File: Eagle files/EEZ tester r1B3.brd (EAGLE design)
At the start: 84 x 76 mm, 91 parts, among them IC2 LM5574MTX/NOPB, K1 RT314005, Q1 2N7002, Q2 2N7002, Q3 2N7002, Q4 2N7002, Q5 2N7002, Q6 2N7002, SW1 1301.9316, SW2 1301.9316, X1 39303035, X3 SSW-113-02-S-D-RA, X4 ???, X6 09185166324

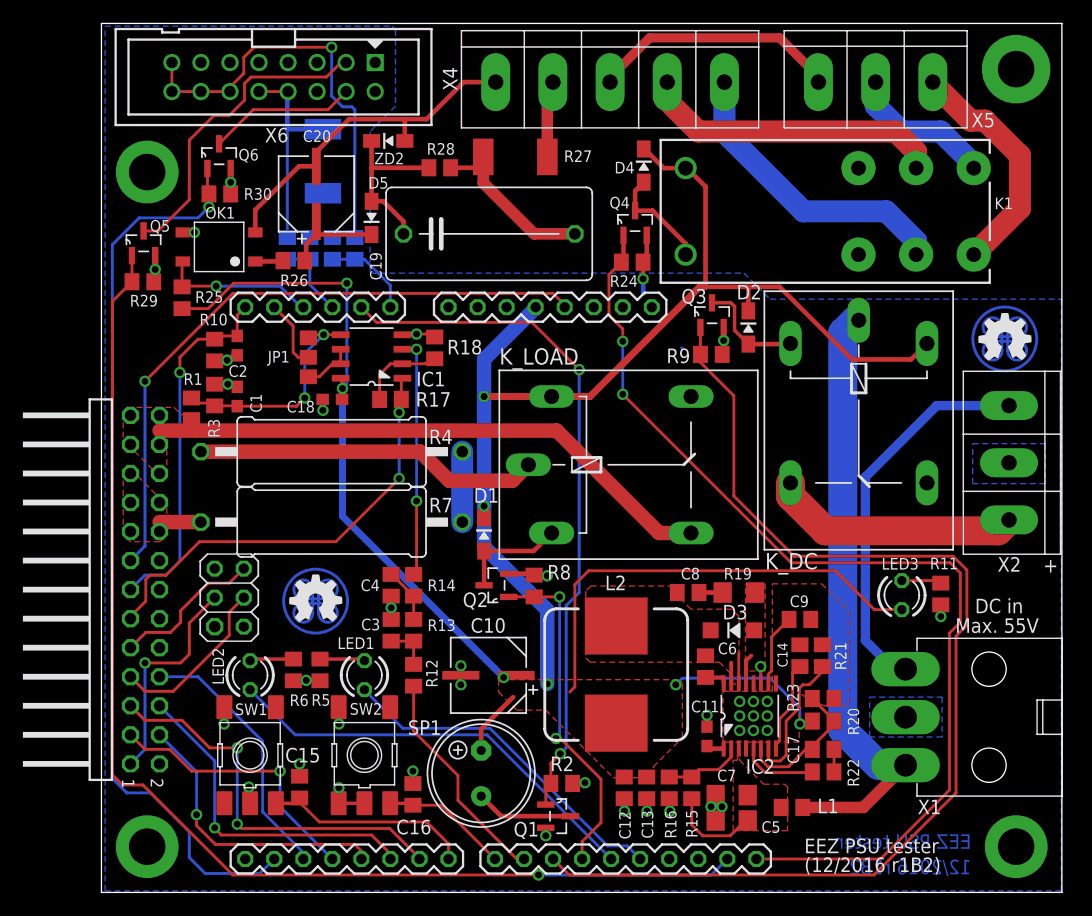
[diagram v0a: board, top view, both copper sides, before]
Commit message: Arduino rotated ICSP fixed
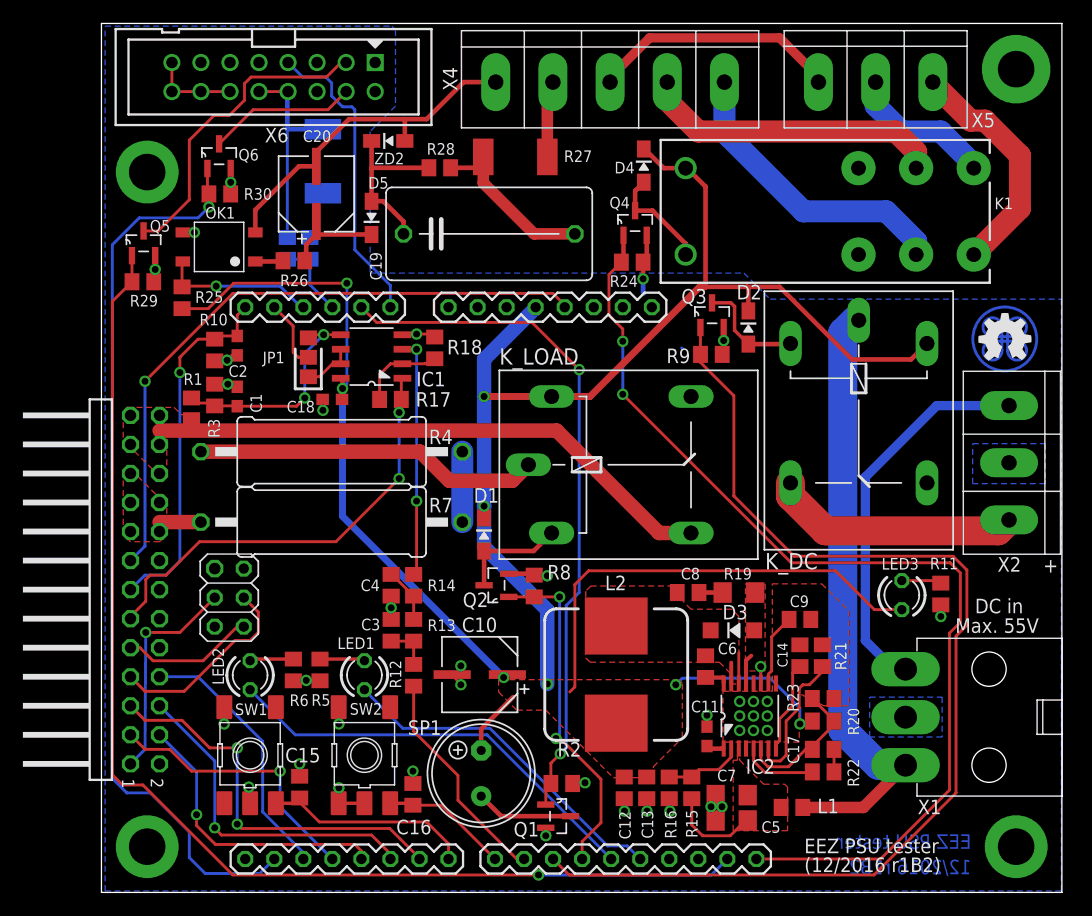
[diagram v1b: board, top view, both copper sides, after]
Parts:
- removed EEZ_SIGNATURE: SIGNATURESMALL, EEZ_Lib1:SIGNATURE_5MM
- removed R31: 10K, rcl:R0805
- removed R32: 3K2, rcl:R0805
- C17: value 4n7 -> 6n8
- C20: value 47u -> 220u
- L2: value 100uH -> 220uH
- R17: value (none) -> 10K
- R18: value (none) -> 20K
- R21: value 30K -> 18K
- R22: value 11K -> 20K
- R25: value 1K -> 2K2
- R26: value 330R -> 300R
- moved C10 0.76 mm to (33.1, 35.1)
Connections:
- net N$12 renamed LED_GREEN
- net N$14 renamed LED_RED
- net N$17 renamed SW2
- net N$18 renamed DC_ENABLE
- net N$6 renamed RPROG
- net N$8 renamed LOAD_ENABLE
- removed net +12V_AUX: MCU.A0, R31.1, R32.2
- new net AUX_DOUT2: MCU.A0, X6.7
- net GND: no longer R32.1
- net N$38: no longer R31.2
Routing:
- net N$38: track 37.1 -> 7.62 mm, vias 1 -> 0
- net AUX_DOUT2: track 0.00 -> 26.8 mm
- net +12V_AUX: track 7.93 -> 0.00 mm
- net MISO: track 15.0 -> 17.4 mm
- net SCLK: track 13.4 -> 11.6 mm
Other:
- board text removed: "R31"
- board text removed: "R32"

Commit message: parts value corrections
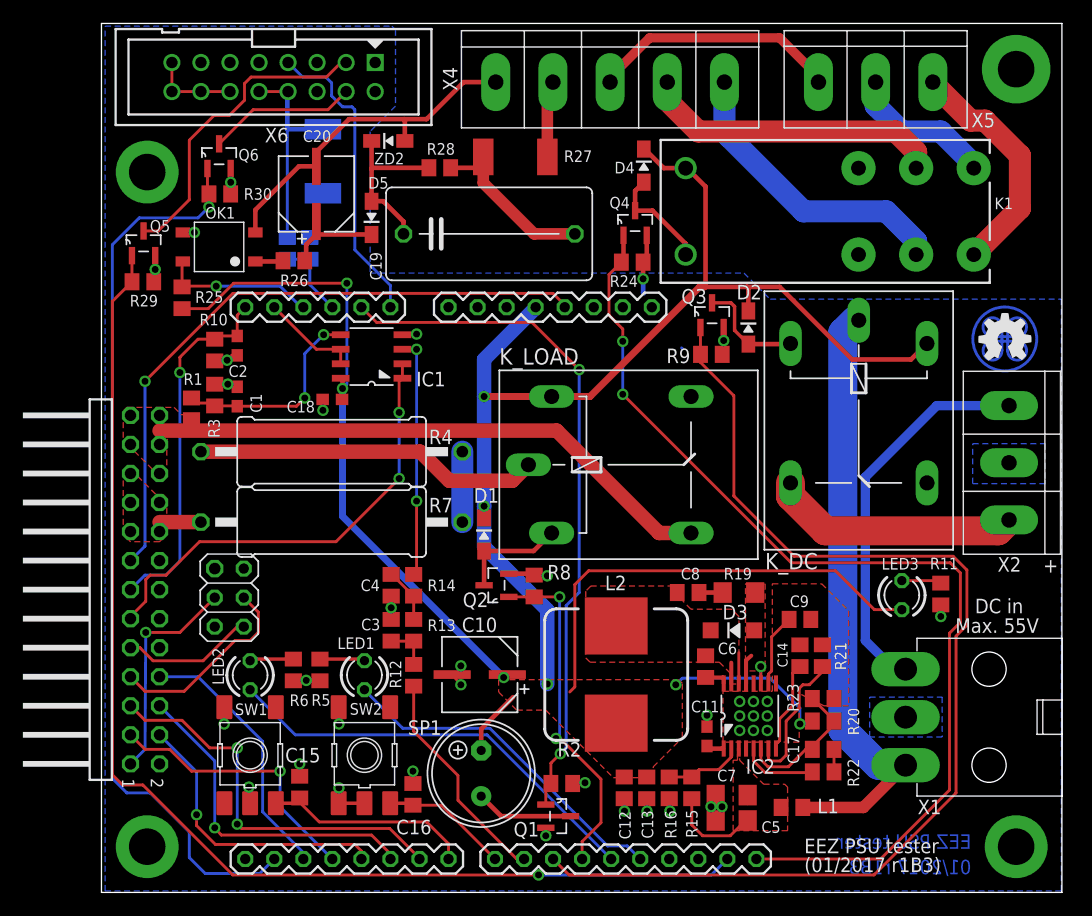
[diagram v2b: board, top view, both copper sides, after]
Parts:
- removed JP1: 0R-JUMPA, jump-0r-smd:A0R-JMP
- removed R17: 10K, rcl:R0805
- removed R18: 20K, rcl:R0805
- C3, C4: value 4n7 -> 2u2
- IC1: value (none) -> LM358
- R11: value ??? -> 300R
- R12, R13, R14: value 1K -> 5K1
- X2, X5: value (none) -> 282836-3
- X4: value ??? -> 282836-5
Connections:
- net !INT renamed !PB_INT_ADC
- net !RESET_OUT renamed !PB_RESET_OUT
- net +5V_AUX renamed VCC_AUX
- net CS_ADC renamed PB_ADC
- net CS_DAC renamed PB_DAC
- net CS_EXPANDER renamed PB_EXPANDER
- net NTC renamed PB_NTC
- removed net N$11: C15.1, MCU.7, SW1.3, SW1.4
- removed net N$223: IC1.2, R17.1, R18.1
- removed net N$5: IC1.6, IC1.7, JP1.3
- removed net OUT_MON: JP1.2, MCU.A4
- new net PB_OUT_MON: IC1.6, IC1.7, MCU.A4
- new net SW: C6.1, C8.1, D3.C, IC2.14, IC2.15, L2.1
- net AUX_USET: now also IC1.2; no longer R17.2
- net GND: no longer R18.2
- net N$7: no longer JP1.1
- net SW1: now also C15.1, MCU.7, SW1.3, SW1.4; no longer C6.1, C8.1, D3.C, IC2.14, IC2.15, L2.1
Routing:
- net N$11: track 18.4 -> 0.00 mm
- net SW1: track 4.51 -> 18.4 mm
- net PB_OUT_MON: track 0.00 -> 8.61 mm
- net N$223: track 7.49 -> 0.00 mm
- net OUT_MON: track 6.14 -> 0.00 mm
- net N$5: track 4.56 -> 0.00 mm
- net SW: track 0.00 -> 4.51 mm
- net GND: track 50.3 -> 48.7 mm
- net N$7: track 19.7 -> 18.2 mm
- net AUX_USET: track 38.7 -> 40.0 mm
- added copper zone on layer 1, net SW
- removed copper zone on layer 1, net SW1
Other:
- board text added: "(01/2017 r1B3)"
- board text added: "01/2017 r1B3"
- board text removed: "(12/2016 r1B2)"
- board text removed: "12/2016 r1B2"
- board text removed: "JP1"
- board text removed: "R17"
- board text removed: "R18"

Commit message: pinout redefinition
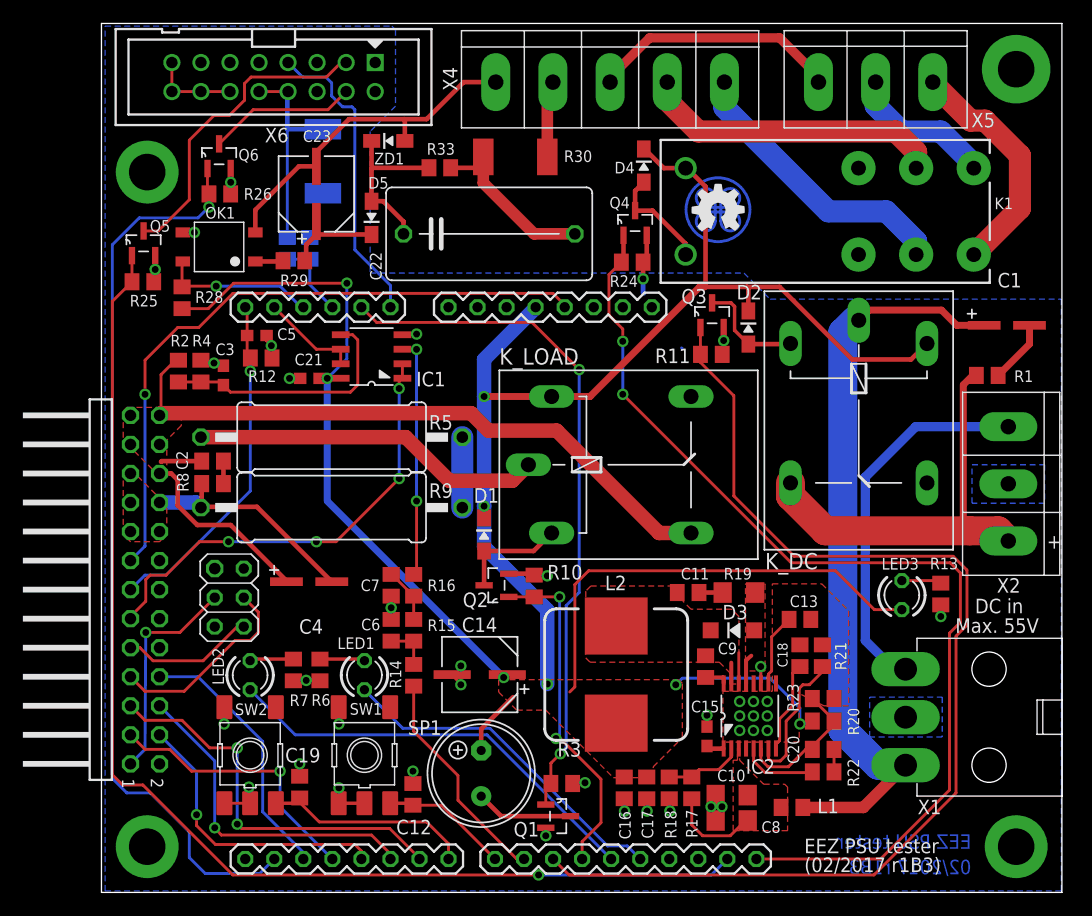
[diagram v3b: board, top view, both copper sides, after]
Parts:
- added C21: 100n, rcl:C0603
- added C22: 220n, rcl:C150-084X183
- added C23: 220u, EEZ_Lib1:CAPAE660X610N
- added R17: 47K, rcl:R0805
- added R18: 2K2, rcl:R0805
- C1: value 100n -> 10u; device rcl:C0603 -> MyLib6:PANASONIC_C
- C10: value 47u -> 1u/100V; device EEZ_Lib1:CAPAE660X610N -> rcl:C1206
- C11: value 100n -> 330p; device rcl:C0603 -> rcl:C0805
- C12: value 2u2 -> 10n
- C13: value n.c. -> 10n
- C14: value 1n -> 47u; device rcl:C0805 -> EEZ_Lib1:CAPAE660X610N
- C15: value 10n -> 100n; device rcl:C0805 -> rcl:C0603
- C16: value 10n -> 2u2
- C17: value 6n8 -> n.c.
- C18: value 100n -> 1n; device rcl:C0603 -> rcl:C0805
- C19: value 220n -> 10n; device rcl:C150-084X183 -> rcl:C0805
- C2: value 100n -> 470n; device rcl:C0603 -> rcl:C0805
- C20: value 220u -> 6n8; device EEZ_Lib1:CAPAE660X610N -> rcl:C0805
- C3: value 2u2 -> 100n; device rcl:C0805 -> rcl:C0603
- C4: value 2u2 -> 10u; device rcl:C0805 -> MyLib6:PANASONIC_C
- C5: value 1u/100V -> 100n; device rcl:C1206 -> rcl:C0603
- C6: value 22n -> 2u2
- C7: value 1u/100V -> 2u2; device rcl:C1206 -> rcl:C0805
- C8: value 330p -> 1u/100V; device rcl:C0805 -> rcl:C1206
- C9: value 10n -> 22n
- IC1: value LM358 -> OPA2344
- R1: value 68K -> 33R
- R10: value 4K7 -> 100K
- R11, R26: value 300R -> 100K
- R12: value 5K1 -> 4K7
- R13: value 5K1 -> 300R
- R15: value 47K -> 5K1
- R16: value 2K2 -> 5K1
- R2: value 100K -> 68K
- R25: value 2K2 -> 100K
- R27: value 330R/2W -> 2K2; device rcl:R2512 -> rcl:R0805
- R28: value 1M -> 2K2
- R29: value 100K -> 200R
- R3: value 7K5 -> 100K
- R30: value 100K -> 330R/2W; device rcl:R0805 -> rcl:R2512
- R33: value 2K2 -> 1M
- R4: value 150R/2W -> 7K5; device rcl:0617/22 -> rcl:R0805
- R5: value 330R -> 150R/2W; device rcl:R0805 -> rcl:0617/22
- R7: value 150R/2W -> 330R; device rcl:0617/22 -> rcl:R0805
- R8: value 100K -> 1R
- R9: value 100K -> 150R/2W; device rcl:R0805 -> rcl:0617/22
- moved R1 69.7 mm to (77.5, 61.2), turned to 180 degrees
- moved C1 67.6 mm to (79.2, 65.6), turned to 0 degrees
- moved C20 65.8 mm to (63.1, 28.5), turned to 0 degrees
- moved C5 59.4 mm to (13.6, 64.7)
- moved C19 51.1 mm to (17.3, 25.2), turned to 90 degrees
- moved R2 49.2 mm to (6.73, 61.6), turned to 270 degrees
- moved C18 46.6 mm to (61.1, 36.7), turned to 270 degrees
- moved R13 46.2 mm to (73.4, 42.1), turned to 90 degrees
- moved R3 45.6 mm to (40.3, 25.5), turned to 180 degrees
- moved C15 35.9 mm to (53.0, 29.7), turned to 270 degrees
- moved R9 35.8 mm to (20.1, 49.7), turned to 0 degrees
- moved C7 35.0 mm to (25.3, 42.9), turned to 270 degrees
- moved R10 34.7 mm to (37.8, 42.8)
- moved R12 30.8 mm to (14.0, 62.7), turned to 0 degrees
- moved R8 29.5 mm to (9.72, 51.8), turned to 0 degrees
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- renumbered R34 to R32, R35 to R31, ZD2 to ZD1
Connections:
- removed net DC_ENABLE: MCU.10, Q3.1, R9.2
- removed net LOAD_ENABLE: MCU.11, Q2.1, R8.2
- new net N$5: C1.2, R1.1
- new net N$94: C2.2, R8.2
- new net PB_LOAD: MCU.11, Q2.1, R10.2
- new net PB_POWER: MCU.10, Q3.1, R11.2
- net !PB_RESET_OUT: now also MCU.6, X3.5; no longer MCU.3, X3.3
- net +5V: now also C14.1, C16.1, C17.1, C21.1, R28.2; no longer C10.1, C12.1, C13.1, C18.1, R25.2
- net AC_AUX: now also R28.1; no longer R25.1
- net AUX_DIR: now also R25.2; no longer R29.2
- net AUX_SS: now also R26.2; no longer R30.2
- net BUZZER: now also R3.2; no longer R2.2
- net DC_IN: now also C1.1
- net DC_OUT: now also R1.2
- net DC_PREG1: now also C10.1, C8.1, R17.2; no longer C5.1, C7.1, R15.2
- net GND: now also C14.2, C15.1, C17.2, C18.1, C19.2, C21.2, C3.1, C5.1, C6.2, C8.2, R10.1, R12.2, R13.1, R18.1, R25.1, R26.1, R3.1, R4.2, R7.2; no longer C1.1, C11.1, C14.1, C15.2, C18.2, C2.1, C3.2, C4.2, C5.2, C9.2, R10.2, R16.1, R2.1, R29.1, R3.2, R30.1, R5.2, R8.1, R9.1
- net MISO: now also MCU.ICSP_MISO, X3.9; no longer MCU.ICSP_SCK, X3.7
- net N$1: now also R5.1, R9.2; no longer R4.1, R7.2
- net N$128: now also C20.1; no longer C17.1
- net N$13: now also C6.1, R14.1, R15.2; no longer C3.1, R12.1, R13.2
- net N$131: now also C9.2; no longer C6.2
- net N$15: now also R6.1; no longer R5.1
- net N$16: now also R7.1; no longer R6.1
- net N$166: now also C15.2; no longer C11.2
- net N$167: now also C18.2; no longer C14.2
- net N$168: now also C13.1; no longer C9.1
- net N$180: now also R17.1, R18.2; no longer R15.1, R16.2
- net N$2: now also R5.2; no longer R4.2
- net N$227: now also R16.1; no longer R14.1
- net N$27: now also R30.1; no longer R27.1
- net N$28: now also C22.2, R30.2, R33.1; no longer C19.2, R27.2, R28.1
- net N$29: now also C22.1, R33.2; no longer C19.1, R28.2
- net N$3: now also R13.2; no longer R11.2
- net N$31: now also C23.2; no longer C20.2
- net N$33: now also R29.2; no longer R26.2
- net N$34: now also C23.1, R29.1; no longer C20.1, R26.1
- net N$37: now also R27.2; no longer R33.2
- net N$46: now also C11.2; no longer C8.2
- net N$7: now also C3.2, R2.2, R4.1; no longer C1.2, R1.2, R3.1
- net N$77: now also C20.2; no longer C17.2
- net N$9: now also C7.1, R15.1, R16.2; no longer C4.1, R13.1, R14.2
- net OUT+: now also C2.1, C4.1, R2.1; no longer R1.1
- net OUT-: now also C4.2, R8.1, R9.1; no longer R7.1
- net PB_EXPANDER: now also MCU.3, X3.3; no longer MCU.6, X3.5
- net PB_NTC: now also C5.2, R12.1; no longer C2.2, R10.1
- net RPROG: now also R14.2; no longer R12.2
- net SCLK: now also MCU.ICSP_SCK, X3.7; no longer MCU.ICSP_MISO, X3.9
- net SW: now also C11.1, C9.1; no longer C6.1, C8.1
- net SW1: now also C19.1, SW2.3, SW2.4; no longer C15.1, SW1.3, SW1.4
- net SW2: now also C12.1, SW1.3, SW1.4; no longer C16.1, SW2.3, SW2.4
- net VCC_AUX: now also R27.1; no longer R33.1
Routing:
- net PB_POWER: track 0.00 -> 97.7 mm
- net DC_ENABLE: track 97.7 -> 0.00 mm
- net PB_LOAD: track 0.00 -> 30.0 mm, vias 0 -> 2
- net LOAD_ENABLE: track 30.0 -> 0.00 mm, vias 2 -> 0
- net OUT+: track 50.2 -> 76.2 mm
- net OUT-: track 3.62 -> 20.0 mm
- net DC_OUT: track 21.9 -> 36.3 mm
- net DC_IN: track 53.9 -> 65.8 mm
- net PB_EXPANDER: track 34.8 -> 24.0 mm, vias 2 -> 1
- net !PB_RESET_OUT: track 24.0 -> 34.8 mm, vias 1 -> 2
- net SCLK: track 11.6 -> 17.4 mm
- net MISO: track 17.4 -> 11.6 mm
- net N$5: track 0.00 -> 5.52 mm
- net N$7: track 18.2 -> 21.9 mm, vias 2 -> 0
- net GND: track 48.7 -> 51.0 mm
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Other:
- board text added: "(02/2017 r1B3)"
- board text added: "02/2017 r1B3"
- board text added: "C21"
- board text added: "C22"
- board text added: "C23"
- board text added: "R17"
- board text added: "R18"
- board text added: "R31"
- board text added: "R32"
- board text added: "ZD1"
- board text removed: "(01/2017 r1B3)"
- board text removed: "01/2017 r1B3"
- board text removed: "R34"
- board text removed: "R35"
- board text removed: "ZD2"
